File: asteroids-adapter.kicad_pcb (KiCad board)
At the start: 2 copper layers, 85.2 x 107.7 mm, 21 parts, among them J1 Asteroids Connector EDAC 307-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, J2 Asteroids harness connector, J3 Audio Gain, U1 TL074

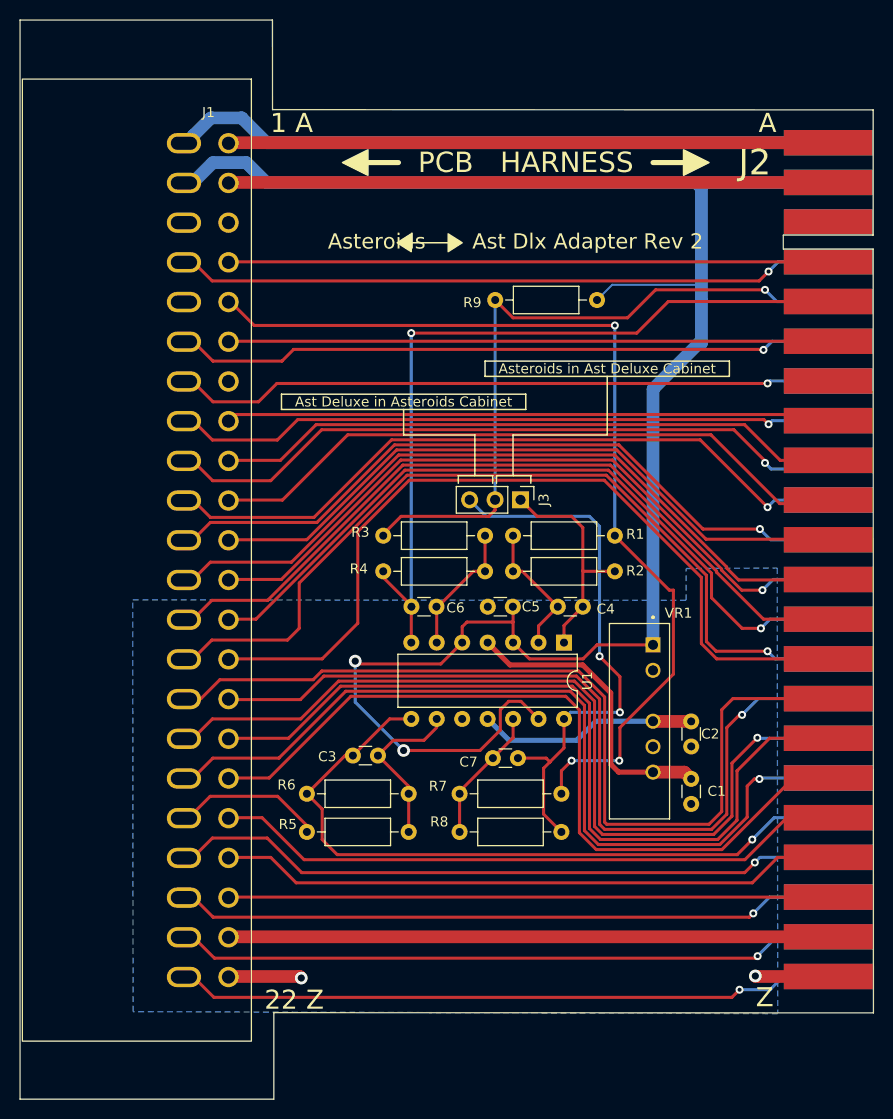
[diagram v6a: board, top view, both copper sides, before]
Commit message: Added FLIP Y jumper
FLIP Y provides required for AST Deluxe in AST cab, and also for
Asteroids in a Deluxe cabaret cabinet.

Added 2-pin header to library

More makefile tweaks.
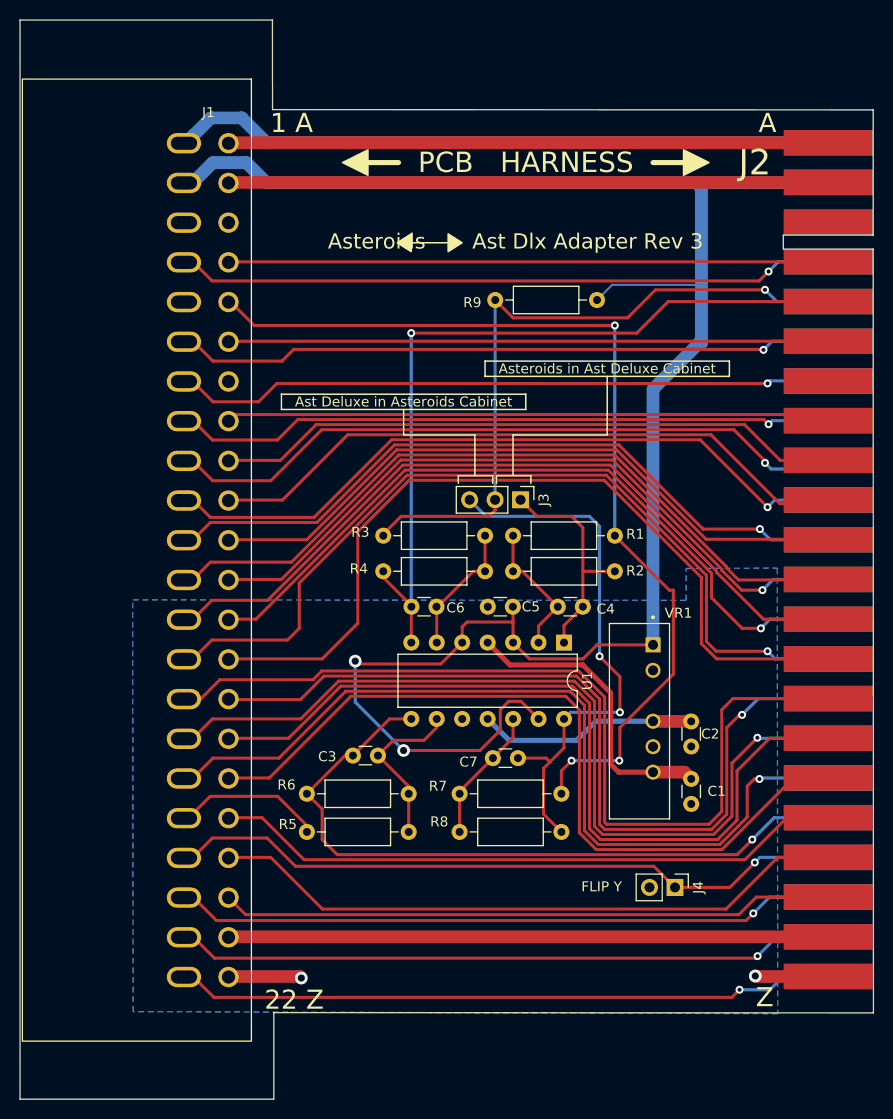
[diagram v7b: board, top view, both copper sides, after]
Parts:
- added J4: FLIP Y, Connector_PinHeader_2.54mm:PinHeader_1x02_P2.54mm_Vertical, F.Cu at (156.4, 130.3)
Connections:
- net Net-(J1-Pad19) renamed /Y_INV
- net Y_INV renamed Y_FLIPPED
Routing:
- net Net-(J1-PadW): track 61.8 -> 64.0 mm
- net Net-(J1-PadX): track 59.8 -> 61.3 mm
- net /Y_INV: track 66.3 -> 67.5 mm

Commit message: More cleanups and bump version
- Cleaned up schematic to align components to grid

- Added bypass cap on 0.1x gain input

- More Makefile cleanups
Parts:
- added C8: Kemet 10 uF 25V MLCC TH, Capacitor_THT:C_Disc_D3.0mm_W1.6mm_P2.50mm, F.Cu at (133.7, 117.2)
- J1: value Asteroids Connector EDAC 307-044-558-201 44-pin edge connector, 0.156" right angle -> Asteroids PCB connector
- moved C7 0.15 mm to (138.2, 117.2)
- moved C3 0.10 mm to (126.7, 117.2)
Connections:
- net /Y_INV renamed Net-(J1-Pad19)
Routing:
- net +5V: track 190.2 -> 190.8 mm, vias 2 -> 1
